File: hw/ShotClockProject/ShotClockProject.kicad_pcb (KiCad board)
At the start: 4 copper layers, 71.8 x 71.8 mm, 117 parts, among them IC1 TP4056-42-ESOP8_Rearanged, J1 USB4120-03-C_REVA, J2 Conn_ST_STDC14, J3 Conn_01x06_Pin, J4 SM03B-SRSS-TB(LF)(SN)(P), J5 Conn_01x02_Pin, J6 Conn_01x03_Pin, Q1 Q_NPN_BCE, Q2 Q_PMOS_SGD, Q3 Q_NPN_BCE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

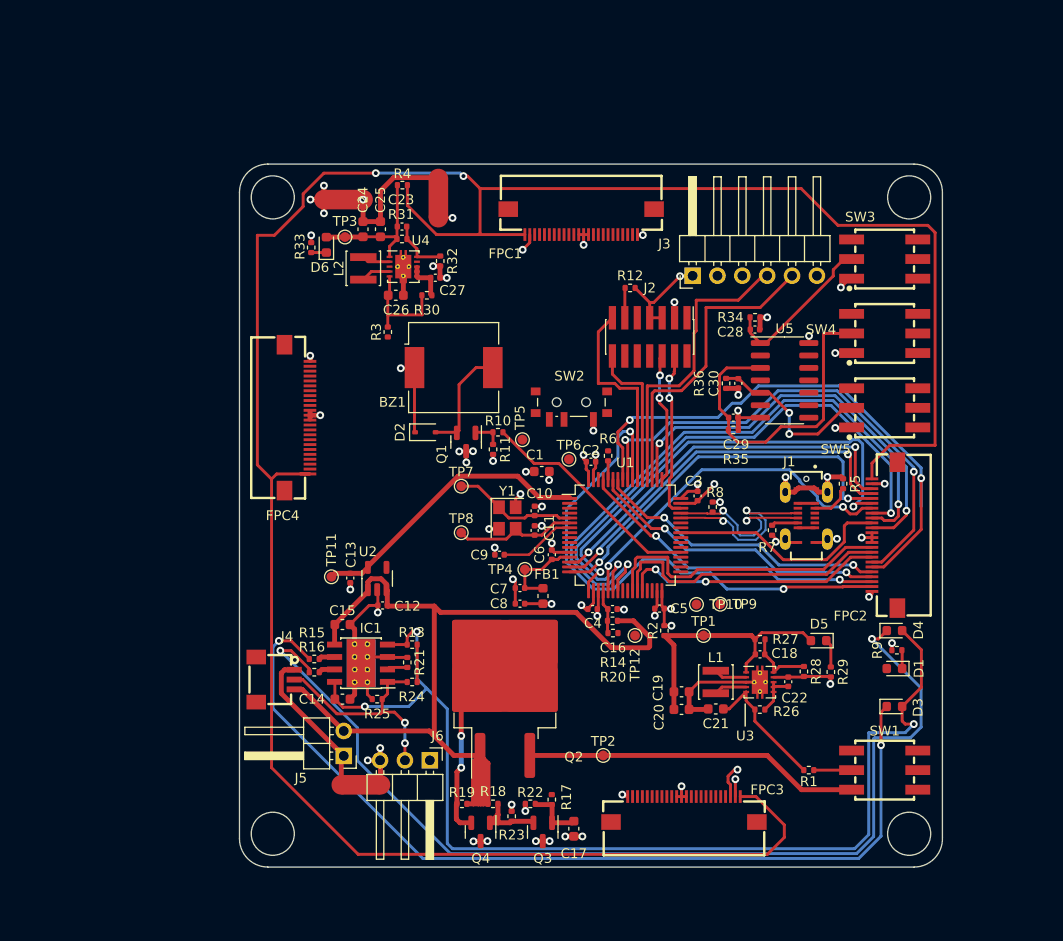
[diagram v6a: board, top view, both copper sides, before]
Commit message: Added USB ESD protection
Removed testpoints for USB+ and USB-
Removed routes to display connectors, for another try
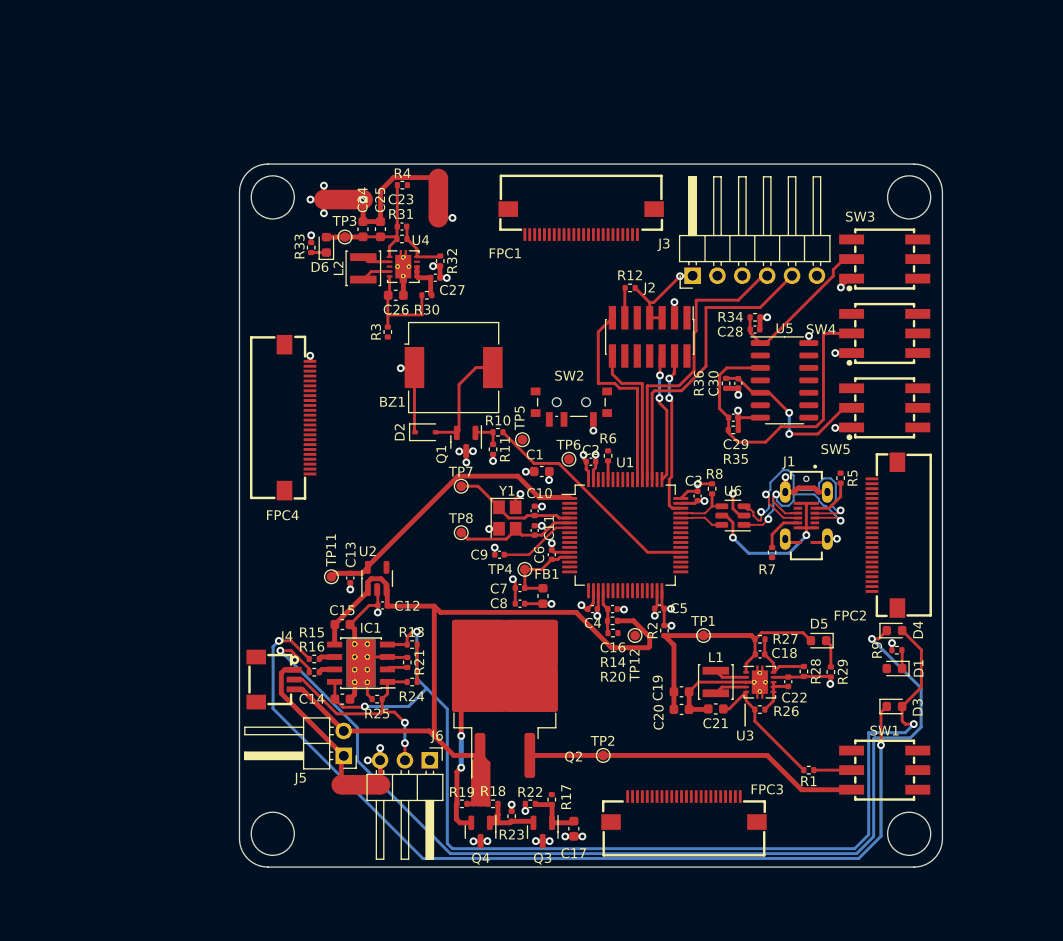
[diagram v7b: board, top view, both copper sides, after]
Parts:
- removed TP10, TP9: TestPoint, TestPoint:TestPoint_Pad_D1.0mm
- added U6: USBLC6-2SC6, Package_TO_SOT_SMD:SOT-23-6, F.Cu at (168.5, 100.0)
- moved R7 2.28 mm to (172.5, 103.8)
- moved R8 1.86 mm to (166.4, 97.3)
- moved R5 0.63 mm to (179.5, 96.2)
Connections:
- J1 pad A6: /STM32F103RCT6/USB_D+ -> /STM32F103RCT6/USB_CONN_D+
- J1 pad A7: /STM32F103RCT6/USB_D- -> /STM32F103RCT6/USB_CONN_D-
- J1 pad B6: /STM32F103RCT6/USB_D+ -> /STM32F103RCT6/USB_CONN_D+
- J1 pad B7: /STM32F103RCT6/USB_D- -> /STM32F103RCT6/USB_CONN_D-
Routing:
- net +5V: track 249.6 -> 0.00 mm, vias 2 -> 0
- net /Connectors to segment displays/DISP1_SEG_G: track 62.9 -> 0.00 mm, vias 2 -> 0
- net /Connectors to segment displays/DISP2_SEG_E: track 60.1 -> 0.00 mm, vias 2 -> 0
- net /Connectors to segment displays/DISP1_SEG_F: track 57.5 -> 0.00 mm, vias 2 -> 0
- net /Connectors to segment displays/TIM2_CH2_PWM2_SEG: track 56.4 -> 0.00 mm, vias 2 -> 0
- net /Connectors to segment displays/DISP2_SEG_D: track 51.0 -> 0.00 mm, vias 2 -> 0
- net /Connectors to segment displays/DISP1_SEG_D: track 48.2 -> 0.00 mm, vias 2 -> 0
- net /Connectors to segment displays/TIM2_CH1_PWM1_SEG: track 43.0 -> 0.00 mm, vias 2 -> 0
- net /Connectors to segment displays/DISP1_SEG_A: track 43.0 -> 0.00 mm, vias 3 -> 0
- net /Connectors to segment displays/DISP1_SEG_C: track 40.1 -> 0.00 mm, vias 2 -> 0
- net /Connectors to segment displays/DISP1_SEG_B: track 39.3 -> 0.00 mm, vias 2 -> 0
- net /Connectors to segment displays/DISP1_SEG_E: track 36.1 -> 0.00 mm, vias 2 -> 0
- net /Connectors to segment displays/DISP2_SEG_DP: track 32.3 -> 0.00 mm, vias 2 -> 0
- net /Connectors to segment displays/DISP2_SEG_G: track 31.2 -> 0.00 mm, vias 2 -> 0
- net /Connectors to segment displays/DISP2_SEG_A: track 30.6 -> 0.00 mm
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
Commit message: Fixed buzzer footprint
Almost done routing, 14 conn left.
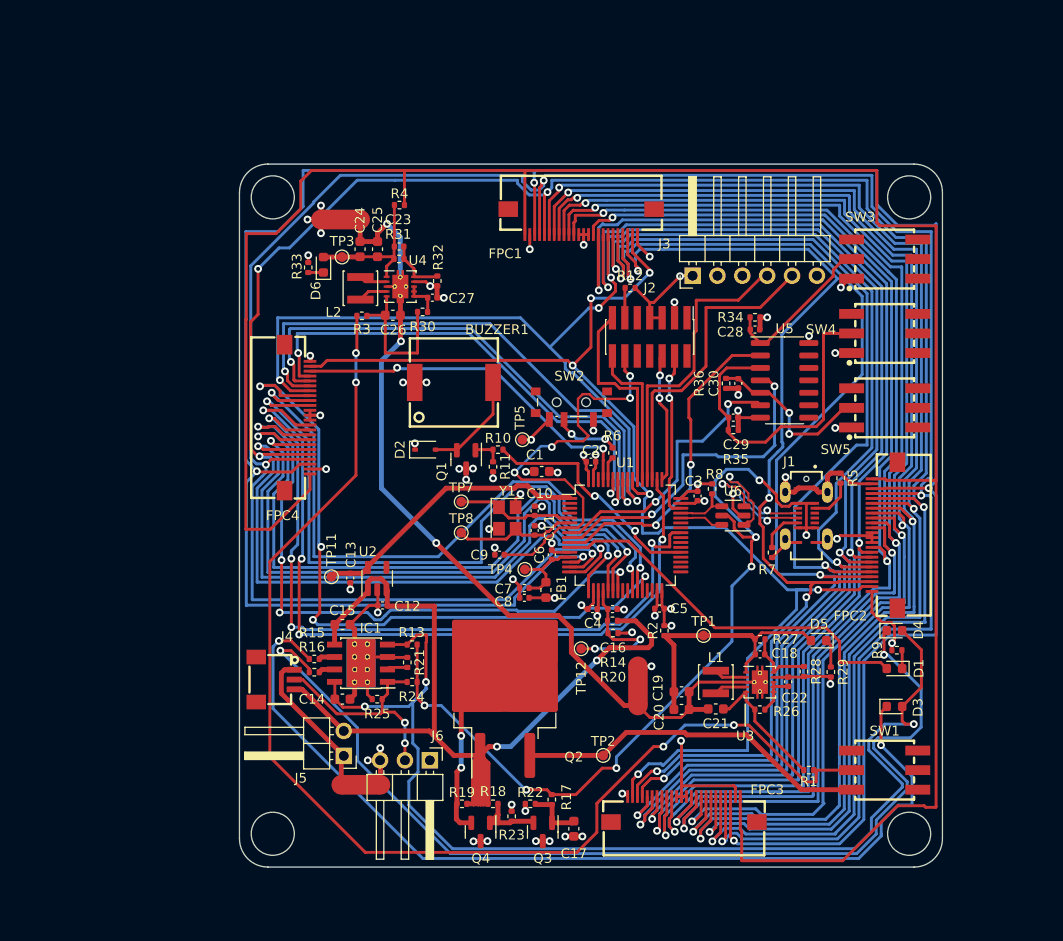
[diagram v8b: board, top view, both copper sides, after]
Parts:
- removed BZ1: Buzzer, Buzzer_Beeper:Buzzer_CUI_CPT-9019S-SMT
- removed TP6: TestPoint, TestPoint:TestPoint_Pad_D1.0mm
- added BUZZER1: CY-SMD-9019-3040, Cy-SMD-9019-3040:BUZ-SMD_L9.0-W9.0-P8.00-LS9.3_CY, F.Cu at (140.0, 86.4)
- moved NT2 53.8 mm to (158.8, 117.4), turned to 90 degrees
- moved TP12 5.66 mm to (153.0, 113.6)
- moved R3 3.12 mm to (130.6, 79.6), turned to 0 degrees
- moved TP3 2.06 mm to (128.6, 73.6)
- moved D6 2.06 mm to (126.7, 74.4)
- moved C27 2.06 mm to (137.8, 77.7)
- moved NT3 2.06 mm to (128.4, 69.8)
- moved C24 2.06 mm to (130.4, 72.8)
- moved C25 2.06 mm to (132.2, 72.8)
- moved C26 2.06 mm to (133.8, 79.5)
- moved L2 2.06 mm to (130.4, 76.8)
- moved R4 2.06 mm to (134.4, 68.3)
- moved U4 2.06 mm to (134.5, 76.6)
- moved R33 2.06 mm to (125.1, 74.7)
- moved C23 2.06 mm to (134.4, 72.5)
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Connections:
- J1 pad A6: /STM32F103RCT6/USB_CONN_D+ -> unconnected-(J1-D1+-PadA6)
- J1 pad A7: /STM32F103RCT6/USB_CONN_D- -> unconnected-(J1-D1--PadA7)
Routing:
- net /Connectors to segment displays/DISP1_SEG_A: track 0.00 -> 262.0 mm, vias 0 -> 5
- net /Connectors to segment displays/DISP1_SEG_B: track 0.00 -> 258.7 mm, vias 0 -> 5
- net /Connectors to segment displays/DISP1_SEG_C: track 0.00 -> 256.8 mm, vias 0 -> 6
- net +5V: track 0.00 -> 225.2 mm
- net /Connectors to segment displays/DISP1_SEG_F: track 0.00 -> 200.6 mm, vias 0 -> 5
- net /Connectors to segment displays/DISP1_SEG_D: track 0.00 -> 200.6 mm, vias 0 -> 5
- net /Connectors to segment displays/DISP1_SEG_E: track 0.00 -> 200.3 mm, vias 0 -> 5
- net /Connectors to segment displays/TIM2_CH1_PWM1_SEG: track 0.00 -> 200.0 mm, vias 0 -> 7
- net /Connectors to segment displays/DISP1_SEG_DP: track 0.00 -> 198.9 mm, vias 0 -> 7
- net /Connectors to segment displays/DISP2_SEG_C: track 0.00 -> 192.1 mm, vias 0 -> 7
- net /Connectors to segment displays/DISP1_SEG_G: track 0.00 -> 191.7 mm, vias 0 -> 7
- net /Connectors to segment displays/DISP2_SEG_B: track 0.00 -> 190.6 mm, vias 0 -> 5
- net /Connectors to segment displays/DISP2_SEG_D: track 0.00 -> 187.7 mm, vias 0 -> 6
- net /Connectors to segment displays/DISP2_SEG_A: track 0.00 -> 185.2 mm, vias 0 -> 5
- net /Connectors to segment displays/DISP2_SEG_F: track 0.00 -> 174.3 mm, vias 0 -> 5
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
